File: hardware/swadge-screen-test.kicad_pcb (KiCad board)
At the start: 2 copper layers, 56.8 x 49.2 mm, 21 parts, among them U2 DISP_OLED_UG-2864HSWEG01

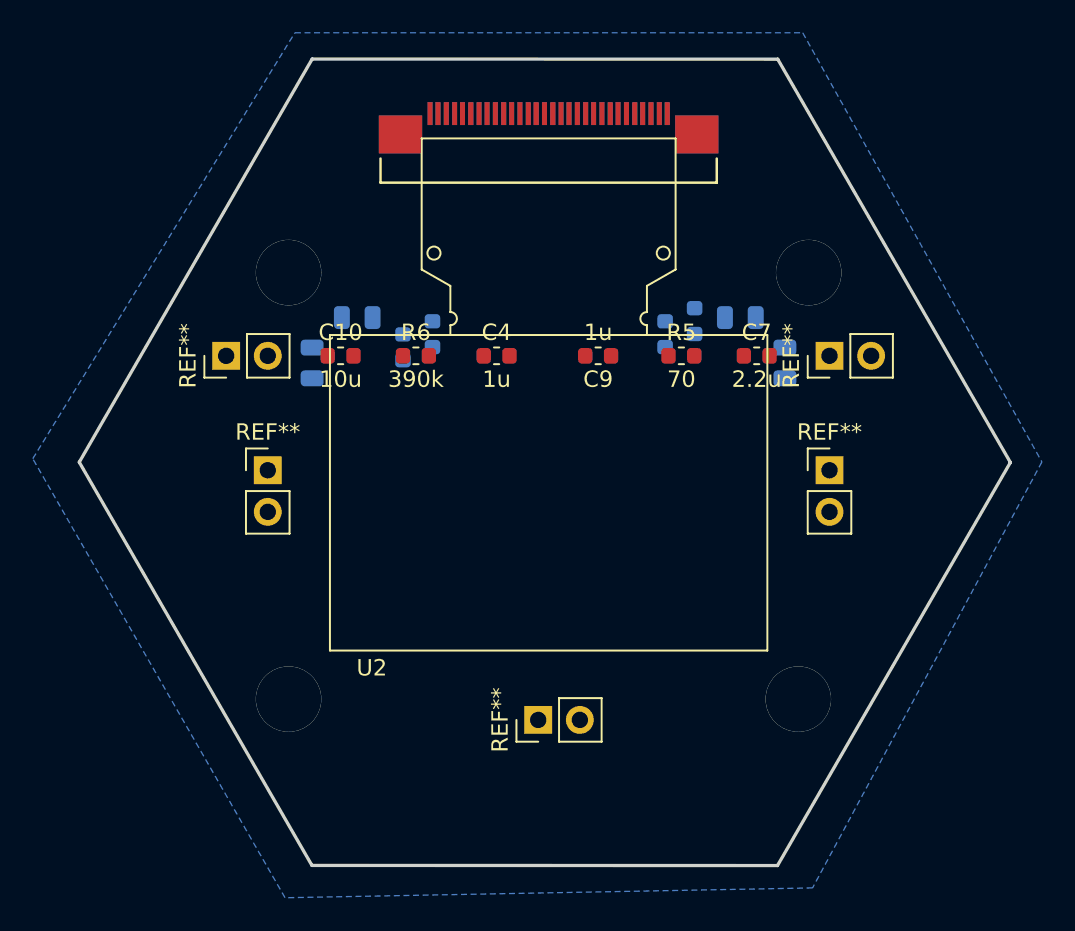
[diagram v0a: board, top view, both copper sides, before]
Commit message: Added copper pour to the front
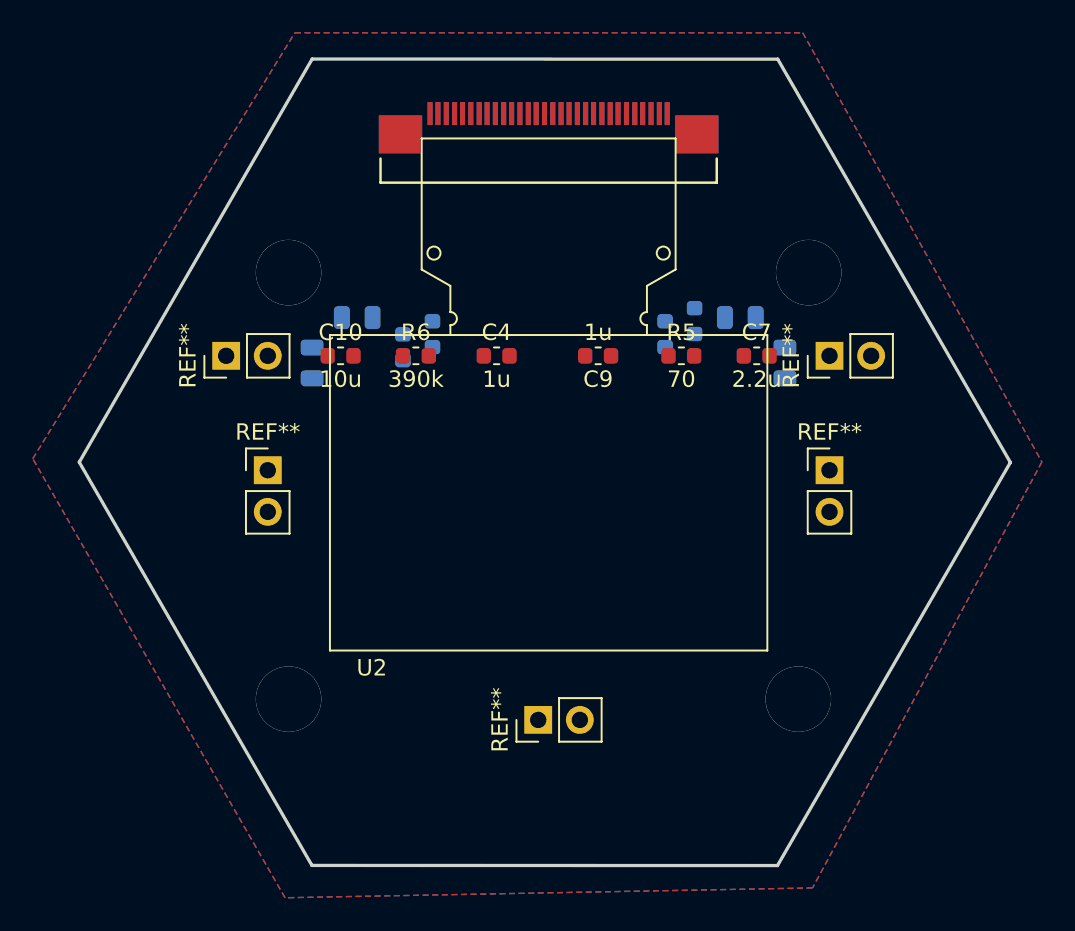
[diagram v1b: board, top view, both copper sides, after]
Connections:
- C9 pad 2: Net-(C9-Pad2) -> GND
- R5 pad 1: Net-(D1-Pad4) -> GND
- U2 pad 31: (no net) -> GND
- U2 pad 32: (no net) -> GND
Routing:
- added copper zone on F.Cu, net GND
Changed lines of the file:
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@@
     (zones 0)
     (modules 21)
-    (nets 15)
+    (nets 14)
   )
   (page A4)
   (layers
-    (0 F.Cu signal hide)
-    (31 B.Cu signal)
+    (0 F.Cu signal)
+    (31 B.Cu signal hide)
     (32 B.Adhes user hide)
     (33 F.Adhes user hide)
-    (34 B.Paste user)
-    (35 F.Paste user hide)
-    (36 B.SilkS user)
-    (37 F.SilkS user hide)
-    (38 B.Mask user)
-    (39 F.Mask user hide)
+    (34 B.Paste user hide)
+    (35 F.Paste user)
+    (36 B.SilkS user hide)
+    (37 F.SilkS user)
+    (38 B.Mask user hide)
+    (39 F.Mask user)
     (40 Dwgs.User user hide)
     (41 Cmts.User user hide)
@@
     (44 Edge.Cuts user)
     (45 Margin user hide)
-    (46 B.CrtYd user)
-    (47 F.CrtYd user hide)
+    (46 B.CrtYd user hide)
+    (47 F.CrtYd user)
     (48 B.Fab user hide)
-    (49 F.Fab user hide)
+    (49 F.Fab user)
   )
   (setup
@@
   (net 7 "Net-(C9-Pad1)")
   (net 8 "Net-(C10-Pad2)")
-  (net 9 "Net-(D1-Pad4)")
-  (net 10 SCL)
-  (net 11 SDA)
-  (net 12 _RES)
-  (net 13 RX)
-  (net 14 "Net-(R6-Pad2)")
+  (net 9 SCL)
+  (net 10 SDA)
+  (net 11 _RES)
+  (net 12 RX)
+  (net 13 "Net-(R6-Pad2)")
   (net_class Default "This is the default net class."
     (clearance 0.2)
@@
     (add_net "Net-(C9-Pad1)")
     (add_net "Net-(C9-Pad2)")
-    (add_net "Net-(D1-Pad4)")
     (add_net "Net-(R6-Pad2)")
     (add_net RX)
@@
       (net 1 GND))
     (pad 20 smd rect (at -2.2606 -13.5164 90) (size 1.397 0.3048) (layers B.Cu B.Paste B.Mask)
-      (net 11 SDA))
+      (net 10 SDA))
     (pad 19 smd rect (at -1.7526 -13.5164 90) (size 1.397 0.3048) (layers B.Cu B.Paste B.Mask)
-      (net 11 SDA))
+      (net 10 SDA))
     (pad 18 smd rect (at -1.2446 -13.5164 90) (size 1.397 0.3048) (layers B.Cu B.Paste B.Mask)
-      (net 10 SCL))
+      (net 9 SCL))
     (pad 1 smd rect (at 7.239 -13.5164 90) (size 1.397 0.3048) (layers B.Cu B.Paste B.Mask)
       (net 1 GND))
@@
       (net 1 GND))
     (pad 14 smd rect (at 0.762 -13.5164 90) (size 1.397 0.3048) (layers B.Cu B.Paste B.Mask)
-      (net 12 _RES))
+      (net 11 _RES))
     (pad 3 smd rect (at 6.2484 -13.5164 90) (size 1.397 0.3048) (layers B.Cu B.Paste B.Mask)
       (net 6 "Net-(C9-Pad2)"))
@@
       (net 5 "Net-(C7-Pad2)"))
     (pad 26 smd rect (at -5.2578 -13.5164 90) (size 1.397 0.3048) (layers B.Cu B.Paste B.Mask)
-      (net 14 "Net-(R6-Pad2)"))
+      (net 13 "Net-(R6-Pad2)"))
     (pad 24 smd rect (at -4.2418 -13.5164 90) (size 1.397 0.3048) (layers B.Cu B.Paste B.Mask)
       (net 1 GND))
@@
       (net 7 "Net-(C9-Pad1)"))
     (pad 2 smd roundrect (at 0.7875 0 180) (size 0.875 0.95) (layers F.Cu F.Paste F.Mask) (roundrect_rratio 0.25)
-      (net 6 "Net-(C9-Pad2)"))
+      (net 1 GND))
     (model ${KIPRJMOD}/kicad-libs/package3d/C_0603_1608Metric.wrl
       (at (xyz 0 0 0))
@@
       (net 1 GND))
     (pad 2 smd roundrect (at 0.7875 0) (size 0.875 0.95) (layers F.Cu F.Paste F.Mask) (roundrect_rratio 0.25)
-      (net 14 "Net-(R6-Pad2)"))
+      (net 13 "Net-(R6-Pad2)"))
     (model ${KIPRJMOD}/kicad-libs/package3d/C_0603_1608Metric.wrl
       (at (xyz 0 0 0))
@@
       (net 1 GND))
     (pad 26 smd rect (at -5.2578 13.5164 90) (size 1.397 0.3048) (layers F.Cu F.Paste F.Mask)
-      (net 14 "Net-(R6-Pad2)"))
+      (net 13 "Net-(R6-Pad2)"))
     (pad 27 smd rect (at -5.7404 13.5164 90) (size 1.397 0.3048) (layers F.Cu F.Paste F.Mask)
       (net 5 "Net-(C7-Pad2)"))
@@
     (pad 13 smd rect (at 1.2446 13.5164 90) (size 1.397 0.3048) (layers F.Cu F.Paste F.Mask)
       (net 1 GND))
-    (pad 31 smd rect (at -9.0424 12.2464 180) (size 2.6416 2.3114) (layers F.Cu F.Paste F.Mask))
+    (pad 31 smd rect (at -9.0424 12.2464 180) (size 2.6416 2.3114) (layers F.Cu F.Paste F.Mask)
+      (net 1 GND))
     (pad 3 smd rect (at 6.2484 13.5164 90) (size 1.397 0.3048) (layers F.Cu F.Paste F.Mask)
       (net 6 "Net-(C9-Pad2)"))
     (pad 14 smd rect (at 0.762 13.5164 90) (size 1.397 0.3048) (layers F.Cu F.Paste F.Mask)
-      (net 12 _RES))
+      (net 11 _RES))
     (pad 15 smd rect (at 0.254 13.5164 90) (size 1.397 0.3048) (layers F.Cu F.Paste F.Mask)
       (net 1 GND))
@@
       (net 1 GND))
     (pad 18 smd rect (at -1.2446 13.5164 90) (size 1.397 0.3048) (layers F.Cu F.Paste F.Mask)
-      (net 10 SCL))
+      (net 9 SCL))
     (pad 19 smd rect (at -1.7526 13.5164 90) (size 1.397 0.3048) (layers F.Cu F.Paste F.Mask)
-      (net 11 SDA))
+      (net 10 SDA))
     (pad 20 smd rect (at -2.2606 13.5164 90) (size 1.397 0.3048) (layers F.Cu F.Paste F.Mask)
-      (net 11 SDA))
+      (net 10 SDA))
     (pad 23 smd rect (at -3.7592 13.5164 90) (size 1.397 0.3048) (layers F.Cu F.Paste F.Mask)
       (net 1 GND))
@@
     (pad 28 smd rect (at -6.2484 13.5164 90) (size 1.397 0.3048) (layers F.Cu F.Paste F.Mask)
       (net 8 "Net-(C10-Pad2)"))
-    (pad 32 smd rect (at 9.0424 12.2464 180) (size 2.6416 2.3114) (layers F.Cu F.Paste F.Mask))
+    (pad 32 smd rect (at 9.0424 12.2464 180) (size 2.6416 2.3114) (layers F.Cu F.Paste F.Mask)
+      (net 1 GND))
     (model ${KIPRJMOD}/kicad-libs/package3d/ssfv30r_3stlf.stp
       (offset (xyz -9.449999999999999 -9.300000000000001 1.9))
@@
     )
     (pad 1 smd roundrect (at -0.7875 0) (size 0.875 0.95) (layers F.Cu F.Paste F.Mask) (roundrect_rratio 0.25)
-      (net 9 "Net-(D1-Pad4)"))
+      (net 1 GND))
     (pad 2 smd roundrect (at 0.7875 0) (size 0.875 0.95) (layers F.Cu F.Paste F.Mask) (roundrect_rratio 0.25)
-      (net 13 RX))
+      (net 12 RX))
     (model ${KIPRJMOD}/kicad-libs/package3d/R_0603_1608Metric.wrl
       (at (xyz 0 0 0))
@@
     (connect_pads (clearance 0.508))
     (min_thickness 0.254)
+    (fill yes (arc_segments 32) (thermal_gap 0.508) (thermal_bridge_width 0.508))
+    (polygon
+      (pts
+        (xy 242.2 77.6) (xy 228.2 103.6) (xy 196 104.2) (xy 180.6 77.4) (xy 196.6 51.4)
+        (xy 227.6 51.4)
+      )
+    )
+  )
+  (zone (net 1) (net_name GND) (layer F.Cu) (hatch edge 0.508)
+    (connect_pads (clearance 0.508))
+    (min_thickness 0.254)
